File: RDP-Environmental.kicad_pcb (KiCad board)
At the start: 2 copper layers, 71.1 x 49.5 mm, 45 parts, among them J1 OPENLOG, J10 Environmental, J11 GPS, J2 MPU, J3 RT1, J4 RT2, J5 RT3, J6 RT4, J7 3.3V, J8 AVR-PDI-6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

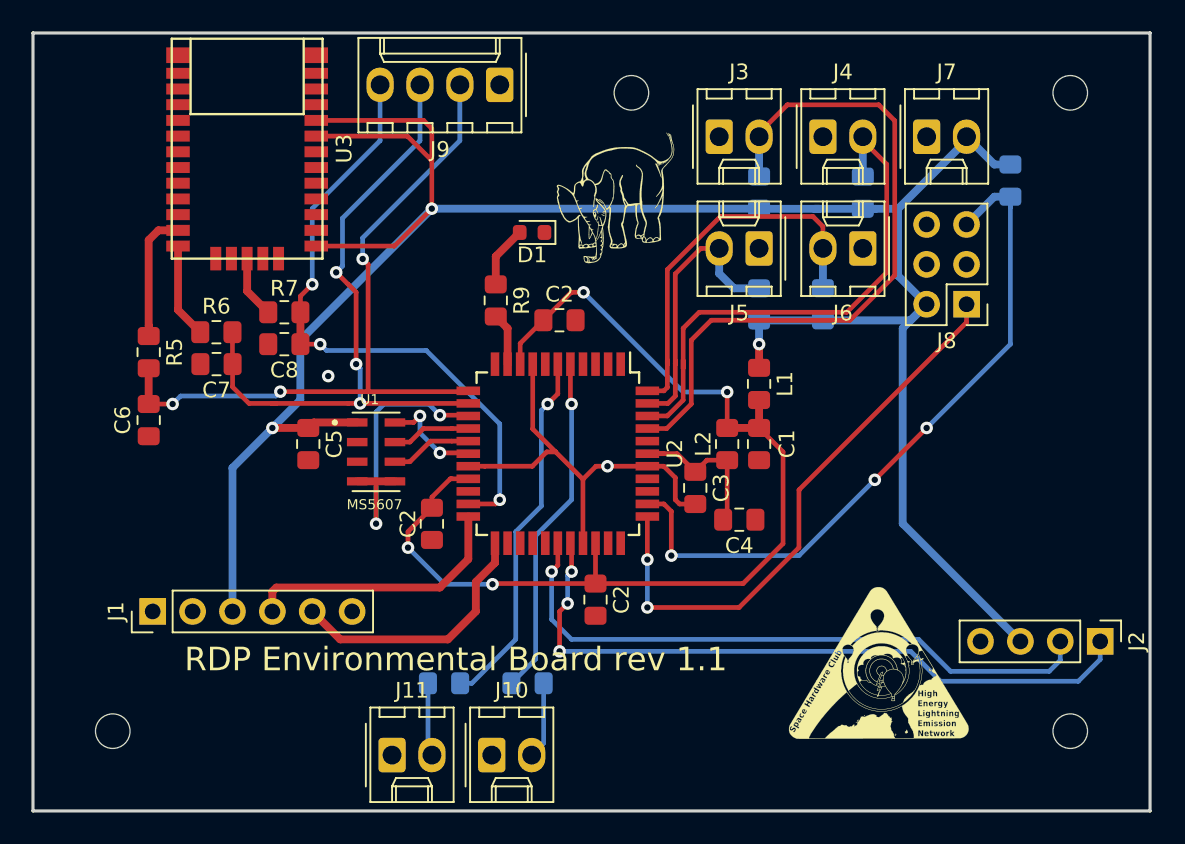
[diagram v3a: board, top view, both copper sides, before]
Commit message: Make holes bigger
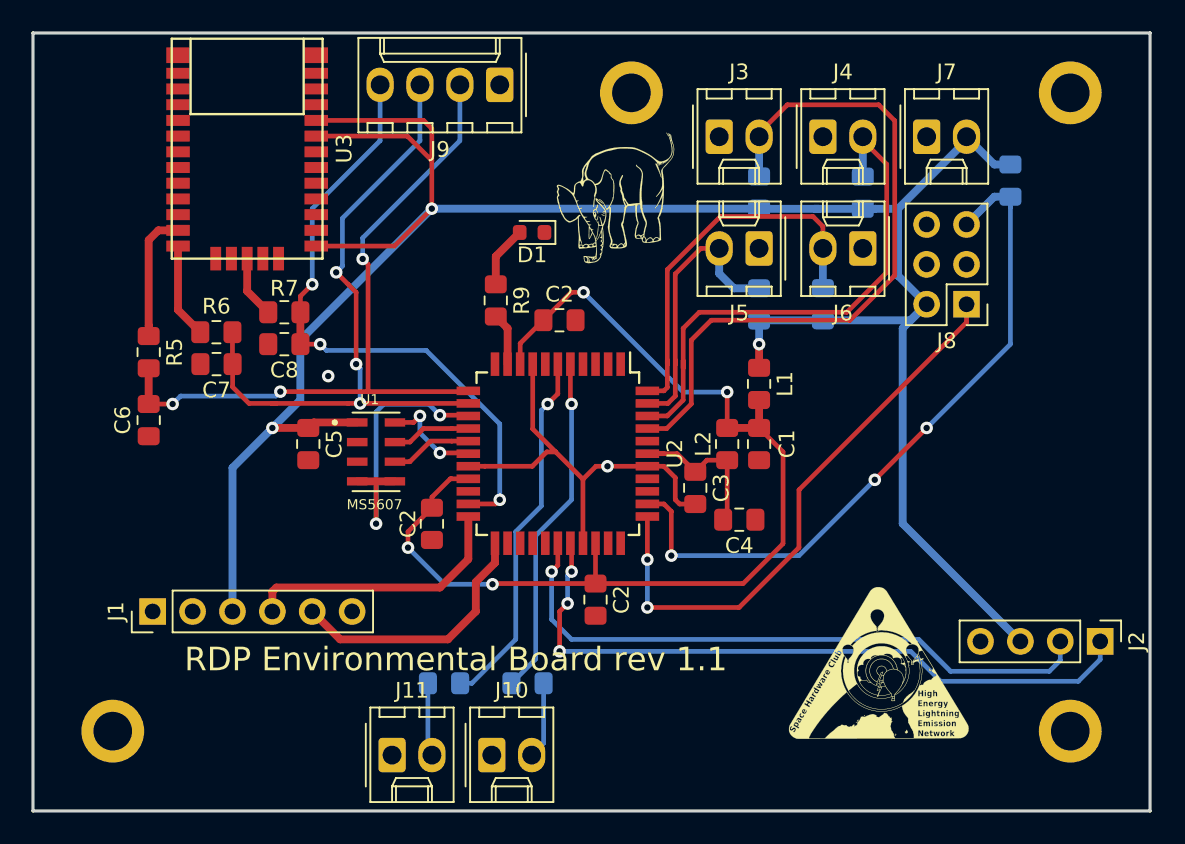
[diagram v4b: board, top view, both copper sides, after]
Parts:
- removed the REF** at (61.0, 25.4)
- removed the REF** at (27.9, 66.0)
- removed the REF** at (88.9, 66.0)
- removed the REF** at (88.9, 25.4)
- added REF**: ScrewHole, rdplibs:ScrewHole, F.Cu at (27.9, 66.0)
- added REF**: ScrewHole, rdplibs:ScrewHole, F.Cu at (61.0, 25.4)
- added REF**: ScrewHole, rdplibs:ScrewHole, F.Cu at (88.9, 25.4)
- added REF**: ScrewHole, rdplibs:ScrewHole, F.Cu at (88.9, 66.0)
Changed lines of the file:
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@@
   )
   (setup
-    (last_trace_width 0.3)
+    (last_trace_width 0.5)
     (user_trace_width 0.25)
     (user_trace_width 0.3)
@@
     (uvia_drill 0.1)
   )
-  (module MountingHole:MountingHole_2.2mm_M2 (layer F.Cu)
-    (at 60.96 25.4 90)
-    (descr "Mounting Hole 2.2mm, no annular, M2")
-    (tags "mounting hole 2.2mm no annular m2")
-    (attr virtual)
-    (fp_text reference REF** (at 0 -3.2 90) (layer F.SilkS) hide
-      (effects (font (size 1 1) (thickness 0.15)))
-    )
-    (fp_text value MountingHole_2.2mm_M2 (at 0 3.2 90) (layer F.Fab) hide
-      (effects (font (size 1 1) (thickness 0.15)))
-    )
-    (fp_circle (center 0 0) (end 2.45 0) (layer F.CrtYd) (width 0.05))
-    (fp_circle (center 0 0) (end 2.2 0) (layer Cmts.User) (width 0.15))
-    (fp_text user %R (at 0.3 0 90) (layer F.Fab) hide
-      (effects (font (size 1 1) (thickness 0.15)))
-    )
-    (pad 1 np_thru_hole circle (at 0 0 90) (size 2.2 2.2) (drill 2.2) (layers *.Cu *.Mask))
-  )
-  (module MountingHole:MountingHole_2.2mm_M2 (layer F.Cu)
-    (at 27.94 66.04 90)
-    (descr "Mounting Hole 2.2mm, no annular, M2")
-    (tags "mounting hole 2.2mm no annular m2")
-    (attr virtual)
-    (fp_text reference REF** (at 0 -3.2 90) (layer F.SilkS) hide
-      (effects (font (size 1 1) (thickness 0.15)))
-    )
-    (fp_text value MountingHole_2.2mm_M2 (at 0 3.2 90) (layer F.Fab) hide
-      (effects (font (size 1 1) (thickness 0.15)))
-    )
-    (fp_circle (center 0 0) (end 2.45 0) (layer F.CrtYd) (width 0.05))
-    (fp_circle (center 0 0) (end 2.2 0) (layer Cmts.User) (width 0.15))
-    (fp_text user %R (at 0.3 0 90) (layer F.Fab) hide
-      (effects (font (size 1 1) (thickness 0.15)))
-    )
-    (pad 1 np_thru_hole circle (at 0 0 90) (size 2.2 2.2) (drill 2.2) (layers *.Cu *.Mask))
-  )
-  (module MountingHole:MountingHole_2.2mm_M2 (layer F.Cu)
-    (at 88.9 66.04 90)
-    (descr "Mounting Hole 2.2mm, no annular, M2")
-    (tags "mounting hole 2.2mm no annular m2")
-    (attr virtual)
-    (fp_text reference REF** (at 0 -3.2 90) (layer F.SilkS) hide
-      (effects (font (size 1 1) (thickness 0.15)))
-    )
-    (fp_text value MountingHole_2.2mm_M2 (at 0 3.2 90) (layer F.Fab) hide
-      (effects (font (size 1 1) (thickness 0.15)))
-    )
-    (fp_text user %R (at 0.3 0 90) (layer F.Fab) hide
-      (effects (font (size 1 1) (thickness 0.15)))
-    )
-    (fp_circle (center 0 0) (end 2.2 0) (layer Cmts.User) (width 0.15))
-    (fp_circle (center 0 0) (end 2.45 0) (layer F.CrtYd) (width 0.05))
-    (pad 1 np_thru_hole circle (at 0 0 90) (size 2.2 2.2) (drill 2.2) (layers *.Cu *.Mask))
-  )
   (module Capacitor_SMD:C_0805_2012Metric_Pad1.15x1.40mm_HandSolder (layer F.Cu)
     (at 65.024 50.555 270)
@@
       (net 1 GND))
   )
-  (module MountingHole:MountingHole_2.2mm_M2 (layer F.Cu)
-    (at 88.9 25.4 90)
-    (descr "Mounting Hole 2.2mm, no annular, M2")
-    (tags "mounting hole 2.2mm no annular m2")
-    (attr virtual)
-    (fp_text reference REF** (at 0 -3.2 90) (layer F.SilkS) hide
-      (effects (font (size 1 1) (thickness 0.15)))
-    )
-    (fp_text value MountingHole_2.2mm_M2 (at 0 3.2 90) (layer F.Fab) hide
-      (effects (font (size 1 1) (thickness 0.15)))
-    )
-    (fp_circle (center 0 0) (end 2.45 0) (layer F.CrtYd) (width 0.05))
-    (fp_circle (center 0 0) (end 2.2 0) (layer Cmts.User) (width 0.15))
-    (fp_text user %R (at 0.3 0 90) (layer F.Fab) hide
-      (effects (font (size 1 1) (thickness 0.15)))
-    )
-    (pad 1 np_thru_hole circle (at 0 0 90) (size 2.2 2.2) (drill 2.2) (layers *.Cu *.Mask))
-  )
   (module rdplibs:HELENlogo (layer F.Cu)
     (at 76.708 61.468)
@@
       (rotate (xyz 0 0 0))
     )
+  )
+  (module rdplibs:ScrewHole (layer F.Cu)
+    (at 27.94 66.04)
+    (descr "Single banana socket, footprint - 6mm drill")
+    (tags "banana socket")
+    (fp_text reference REF** (at 0 -6.5) (layer F.SilkS) hide
+      (effects (font (size 1 1) (thickness 0.15)))
+    )
+    (fp_text value ScrewHole (at -0.25 6.5) (layer F.Fab)
+      (effects (font (size 1 1) (thickness 0.15)))
+    )
+    (fp_text user %R (at 0 0) (layer F.Fab)
+      (effects (font (size 0.8 0.8) (thickness 0.12)))
+    )
+    (fp_circle (center 0 0) (end 2 0) (layer F.Fab) (width 0.1))
+    (pad "" np_thru_hole circle (at 0 0) (size 4 4) (drill 2.46) (layers *.Cu *.Mask))
+    (model ${KISYS3DMOD}/Connector.3dshapes/Banana_Jack_1Pin.wrl
+      (at (xyz 0 0 0))
+      (scale (xyz 2 2 2))
+      (rotate (xyz 0 0 0))
+    )
+  )
+  (module rdplibs:ScrewHole (layer F.Cu)
+    (at 60.96 25.4)
+    (descr "Single banana socket, footprint - 6mm drill")
+    (tags "banana socket")
+    (fp_text reference REF** (at 0 -6.5) (layer F.SilkS) hide
+      (effects (font (size 1 1) (thickness 0.15)))
+    )
+    (fp_text value ScrewHole (at -0.25 6.5) (layer F.Fab)
+      (effects (font (size 1 1) (thickness 0.15)))
+    )
+    (fp_text user %R (at 0 0) (layer F.Fab)
+      (effects (font (size 0.8 0.8) (thickness 0.12)))
+    )
+    (fp_circle (center 0 0) (end 2 0) (layer F.Fab) (width 0.1))
+    (pad "" np_thru_hole circle (at 0 0) (size 4 4) (drill 2.46) (layers *.Cu *.Mask))
+    (model ${KISYS3DMOD}/Connector.3dshapes/Banana_Jack_1Pin.wrl
+      (at (xyz 0 0 0))
+      (scale (xyz 2 2 2))
+      (rotate (xyz 0 0 0))
+    )
+  )
+  (module rdplibs:ScrewHole (layer F.Cu)
+    (at 88.9 25.4)
+    (descr "Single banana socket, footprint - 6mm drill")
+    (tags "banana socket")
+    (fp_text reference REF** (at 0 -6.5) (layer F.SilkS) hide
+      (effects (font (size 1 1) (thickness 0.15)))
+    )
+    (fp_text value ScrewHole (at -0.25 6.5) (layer F.Fab)
+      (effects (font (size 1 1) (thickness 0.15)))
+    )
+    (fp_text user %R (at 0 0) (layer F.Fab)
+      (effects (font (size 0.8 0.8) (thickness 0.12)))
+    )
+    (fp_circle (center 0 0) (end 2 0) (layer F.Fab) (width 0.1))
+    (pad "" np_thru_hole circle (at 0 0) (size 4 4) (drill 2.46) (layers *.Cu *.Mask))
+    (model ${KISYS3DMOD}/Connector.3dshapes/Banana_Jack_1Pin.wrl
+      (at (xyz 0 0 0))
+      (scale (xyz 2 2 2))
+      (rotate (xyz 0 0 0))
+    )
+  )
+  (module rdplibs:ScrewHole (layer F.Cu)
+    (at 88.9 66.04)
+    (descr "Single banana socket, footprint - 6mm drill")
+    (tags "banana socket")
+    (fp_text reference REF** (at 0 -6.5) (layer F.SilkS) hide
+      (effects (font (size 1 1) (thickness 0.15)))
+    )
+    (fp_text value ScrewHole (at -0.25 6.5) (layer F.Fab)
+      (effects (font (size 1 1) (thickness 0.15)))
+    )
+    (fp_text user %R (at 0 0) (layer F.Fab)
+      (effects (font (size 0.8 0.8) (thickness 0.12)))
+    )
+    (fp_circle (center 0 0) (end 2 0) (layer F.Fab) (width 0.1))
+    (pad "" np_thru_hole circle (at 0 0) (size 4 4) (drill 2.46) (layers *.Cu *.Mask))
+    (model ${KISYS3DMOD}/Connector.3dshapes/Banana_Jack_1Pin.wrl
+      (at (xyz 0 0 0))
+      (scale (xyz 2 2 2))
+      (rotate (xyz 0 0 0))
+    )
